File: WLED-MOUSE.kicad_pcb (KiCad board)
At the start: 4 copper layers, 58.2 x 59.4 mm, 20 parts, among them J1 FTDI-header, J2 Power-in, J4 Pixel-strip, J6 Pixel-strip, J7 Pixel-strip, J8 Pixel-strip, M1 INMP441, M2 INMP441-TH, SW1 SW_MEC_5E, SW2 SW_MEC_5E, U1 ESP32-WROOM-32D, U2 ESP32-WROOM-32D, U3 SN74LV4T125

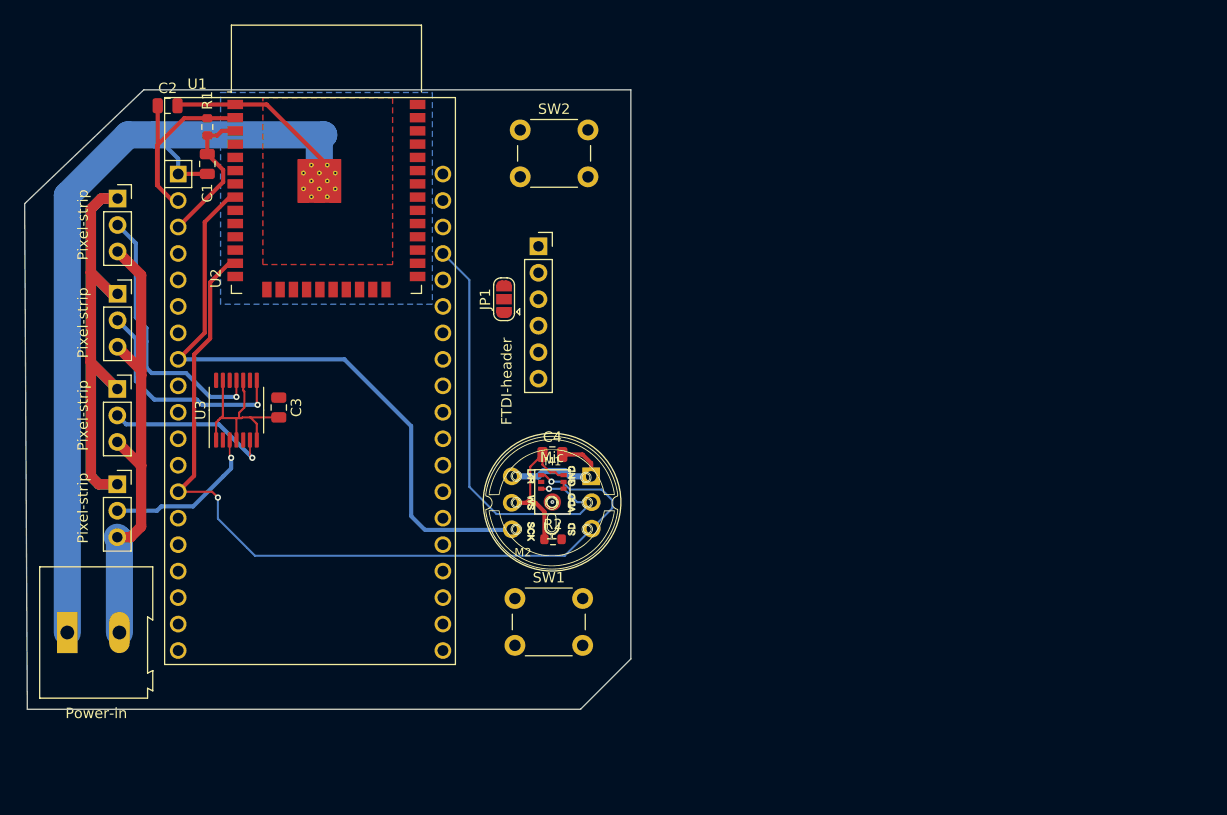
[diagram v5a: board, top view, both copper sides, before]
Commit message: added GPIO names, to silk screen, to make life easier when using the board.
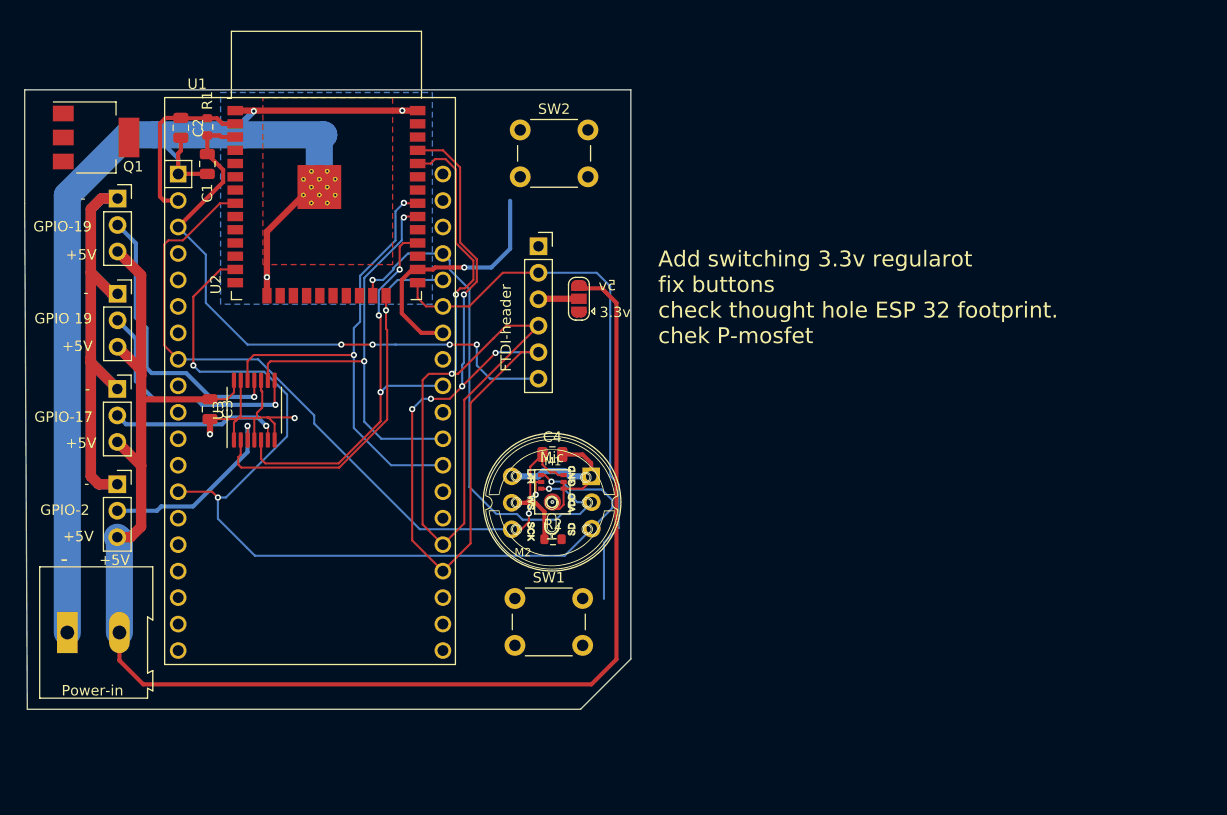
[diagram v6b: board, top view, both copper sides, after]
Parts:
- added Q1: NDT3055L, Package_TO_SOT_SMD:SOT-223-3_TabPin2, F.Cu at (160.3, 84.3)
- SW1, SW2: footprint Button_Switch_THT:SW_PUSH_6mm_H5mm -> Button_Switch_THT:SW_PUSH_6mm
- moved JP1 7.19 mm to (206.6, 99.8)
- moved C3 6.60 mm to (171.2, 110.4)
- moved C2 2.47 mm to (168.4, 83.4), turned to -90 degrees
- moved U3 1.71 mm to (175.4, 110.5)
- moved U2 0.59 mm to (182.4, 90.0)
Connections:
- J1 pad 4: /Tx -> /Rx
- J1 pad 5: /Rx -> /Tx
- SW1 pad 2: /GPIO-0 -> GND
- SW2 pad 1: unconnected-(SW2-Pad1) -> /Button
- SW2 pad 2: unconnected-(SW2-Pad2) -> GND
- U1 pad 26: unconnected-(U1-Pad26) -> /Button
- U1 pad 29: unconnected-(U1-Pad29) -> /Power Relay Pin
- U2 pad 26: unconnected-(U2-Pad26) -> /Button
- U2 pad 29: unconnected-(U2-Pad29) -> /Power Relay Pin
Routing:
- net +5V: track 46.2 -> 147.5 mm
- net /Tx: track 0.00 -> 83.9 mm, vias 0 -> 5
- net /Rx: track 0.00 -> 80.4 mm, vias 0 -> 2
- net /GPIO-0: track 0.00 -> 53.1 mm
- net /LED-4: track 0.00 -> 47.2 mm, vias 0 -> 2
- net /Reset: track 14.1 -> 58.4 mm, vias 0 -> 4
- net /LED-3: track 0.00 -> 41.7 mm, vias 0 -> 2
- net /LED-2: track 0.00 -> 40.9 mm, vias 0 -> 3
- net /LED-1: track 0.00 -> 38.4 mm, vias 0 -> 1
- net GND: track 132.4 -> 160.7 mm, vias 0 -> 5
- net /Button: track 0.00 -> 24.2 mm, vias 0 -> 1
- net /SCK: track 80.4 -> 90.8 mm, vias 2 -> 3
- net /WS: track 42.1 -> 52.0 mm, vias 1 -> 2
- net +3.3V: track 37.6 -> 31.5 mm
- net Net-(J1-Pad3): track 0.00 -> 3.90 mm
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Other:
- outline, holes or cut-outs redrawn
- board text added: "+5V"
- board text added: "-"
- board text added: "3.3v"
- board text added: "5v"
- board text added: "Add switching 3.3v regularot fix buttons check thought hole ESP 32 footprint. chek P-mosfet"
- board text added: "GPIO 19"
- board text added: "GPIO-17"
- board text added: "GPIO-19"
- board text added: "GPIO-2"
